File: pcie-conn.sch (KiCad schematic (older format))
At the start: 18 parts, among them J2 1-2199230-6

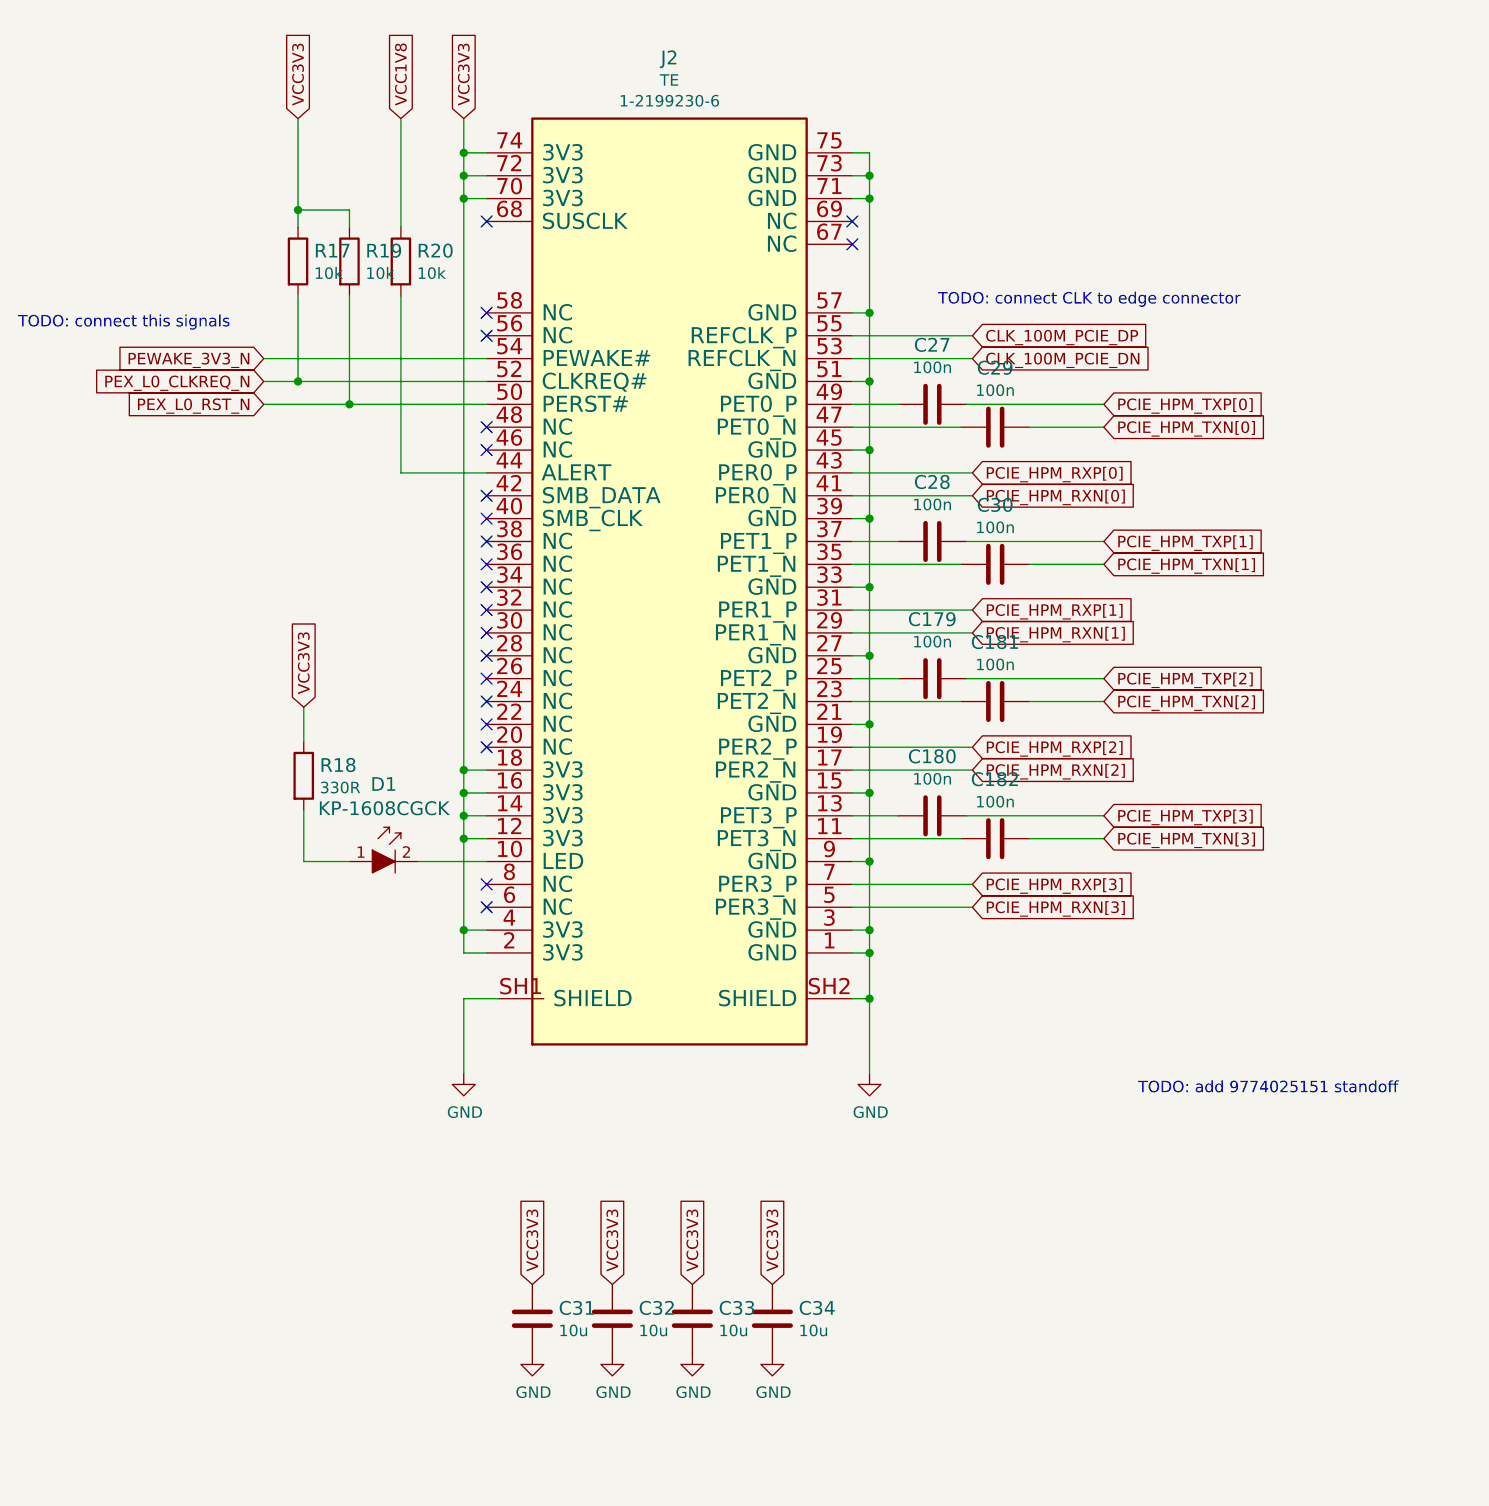
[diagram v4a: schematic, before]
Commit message: Fixes to PCIe connector
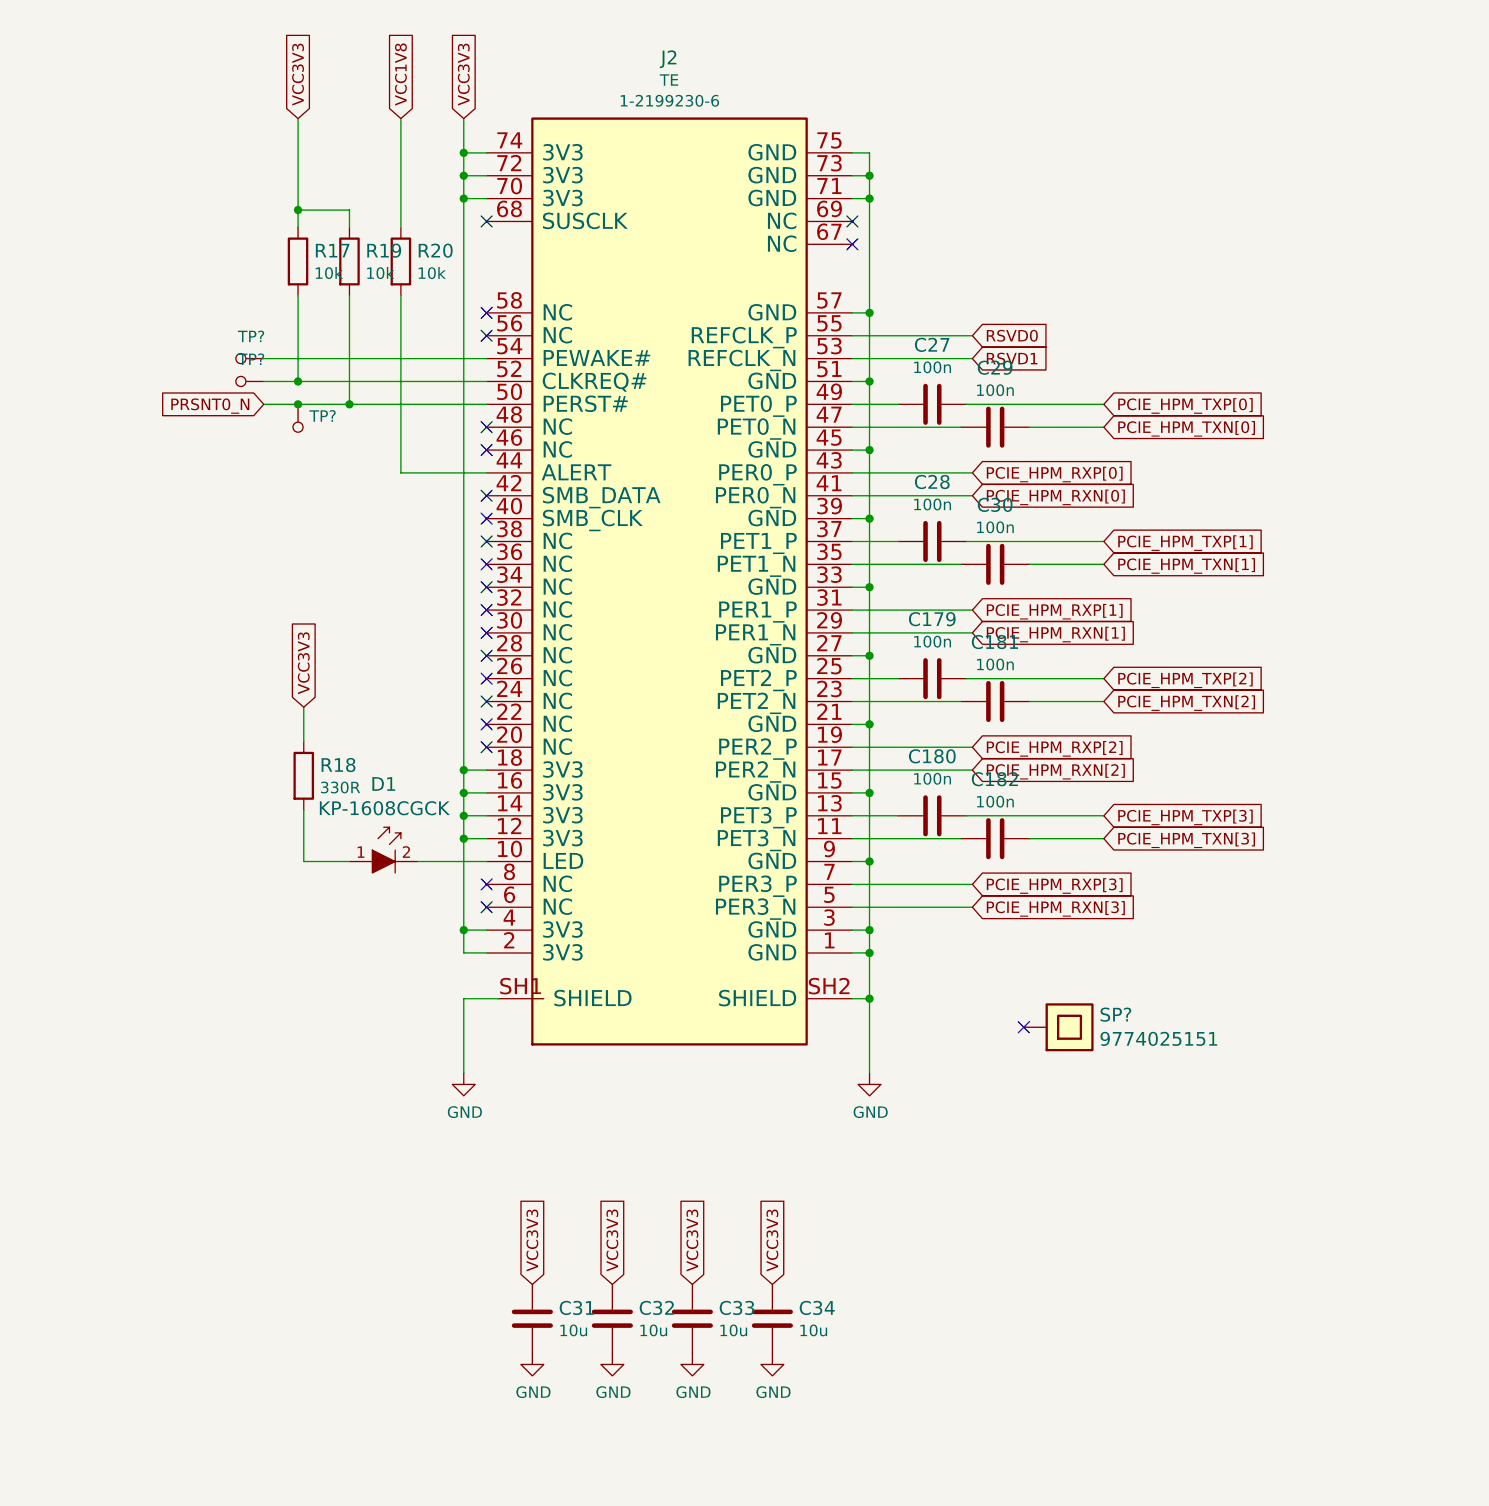
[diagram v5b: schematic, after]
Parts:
- added SP?: 9774025151, antmicro-footprints:9774025151, symbol artix-dc-scm:9774025151
- added TP? (x3): TP_SMD1MM, antmicro-footprints:Testpoint_smd_1mm, symbol artix-dc-scm:TP_SMD1MM
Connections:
- net CLK_100M_PCIE_DN renamed RSVD1
- net CLK_100M_PCIE_DP renamed RSVD0
- net PEWAKE_3V3_N: no longer names the net of J2.54 (PEWAKE#)
- net PEWAKE_3V3_N: now also TP?.1
- net PEX_L0_CLKREQ_N: no longer names the net of J2.52 (CLKREQ#), R17.2
- net PEX_L0_CLKREQ_N: now also TP?.1
- net PEX_L0_RST_N renamed PRSNT0_N
- net PRSNT0_N: now also TP?.1
- no-connect marks 21 -> 22
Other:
- note removed: "TODO: add 9774025151 standoff"
- note removed: "TODO: connect CLK to edge connector\n"
- note removed: "TODO: connect this signals\n"
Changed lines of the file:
@@
 Wire Wire Line
 	7025 3450 7350 3450
-Text GLabel 3675 2550 0    50   Input ~ 0
-PEWAKE_3V3_N
-Text GLabel 3675 2650 0    50   Input ~ 0
-PEX_L0_CLKREQ_N
-Text GLabel 3675 2750 0    50   Input ~ 0
-PEX_L0_RST_N
 Wire Wire Line
 	3675 2550 4650 2550
@@
 	3675 2650 3825 2650
 Wire Wire Line
-	3675 2750 4050 2750
+	3675 2750 3825 2750
 $Comp
 L artix-dc-scm:R_10k_0402 R17
@@
 Text GLabel 5900 6600 1    50   Input ~ 0
 VCC3V3
-Text Notes 7500 5775 0    50   ~ 0
-TODO: add 9774025151 standoff
-Text GLabel 6775 2450 2    50   Input ~ 0
-CLK_100M_PCIE_DP
-Text GLabel 6775 2550 2    50   Input ~ 0
-CLK_100M_PCIE_DN
 NoConn ~ 4650 4950
 NoConn ~ 4650 4850
@@
 Text GLabel 7350 2850 2    50   Input ~ 0
 PCIE_HPM_TXN[0]
-Text Notes 6625 2325 0    50   ~ 0
-TODO: connect CLK to edge connector\n
-Text Notes 2600 2425 0    50   ~ 0
-TODO: connect this signals\n
 Text GLabel 6775 3650 2    50   Input ~ 0
 PCIE_HPM_RXP[1]
@@
 Wire Wire Line
 	7025 4650 7350 4650
+Text GLabel 6775 2450 2    50   Input ~ 0
+RSVD0
+Text GLabel 6775 2550 2    50   Input ~ 0
+RSVD1
+Text GLabel 3675 2750 0    50   Input ~ 0
+PRSNT0_N
+$Comp
+L artix-dc-scm:TP_SMD1MM TP?
+U 1 1 611CC4C6
+P 3575 2550
+F 0 "TP?" V 3480 2597 50  0000 C CNN
+F 1 "TP_SMD1MM" H 3575 2450 50  0001 C CNN
+F 2 "antmicro-footprints:Testpoint_smd_1mm" H 3775 2750 60  0001 L CNN
+F 3 "" H 3775 2850 60  0001 L CNN
+	1    3575 2550
+	0    1    1    0
+$EndComp
+$Comp
+L artix-dc-scm:TP_SMD1MM TP?
+U 1 1 611CCA21
+P 3575 2650
+F 0 "TP?" V 3480 2697 50  0000 C CNN
+F 1 "TP_SMD1MM" H 3575 2550 50  0001 C CNN
+F 2 "antmicro-footprints:Testpoint_smd_1mm" H 3775 2850 60  0001 L CNN
+F 3 "" H 3775 2950 60  0001 L CNN
+	1    3575 2650
+	0    1    1    0
+$EndComp
+$Comp
+L artix-dc-scm:TP_SMD1MM TP?
+U 1 1 611CCE09
+P 3825 2850
+F 0 "TP?" H 3875 2897 50  0000 L CNN
+F 1 "TP_SMD1MM" H 3825 2750 50  0001 C CNN
+F 2 "antmicro-footprints:Testpoint_smd_1mm" H 4025 3050 60  0001 L CNN
+F 3 "" H 4025 3150 60  0001 L CNN
+	1    3825 2850
+	1    0    0    -1
+$EndComp
+Connection ~ 3825 2750
+Wire Wire Line
+	3825 2750 4050 2750
+$Comp
+L artix-dc-scm:9774025151 SP?
+U 1 1 611DD06A
+P 7200 5475
+F 0 "SP?" H 7330 5528 60  0000 L CNN
+F 1 "9774025151" H 7330 5422 60  0000 L CNN
+F 2 "antmicro-footprints:9774025151" H 7200 5475 60  0001 C CNN
+F 3 "" H 7200 5475 60  0001 C CNN
+F 4 "Wurth Elektronik" H 7200 5475 50  0001 C CNN "Manufacturer"
+F 5 "9774025151" H 7200 5475 50  0001 C CNN "MPN"
+	1    7200 5475
+	1    0    0    -1
+$EndComp
+NoConn ~ 7000 5475
 $EndSCHEMATC

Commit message: Fixes after review (pin connections)
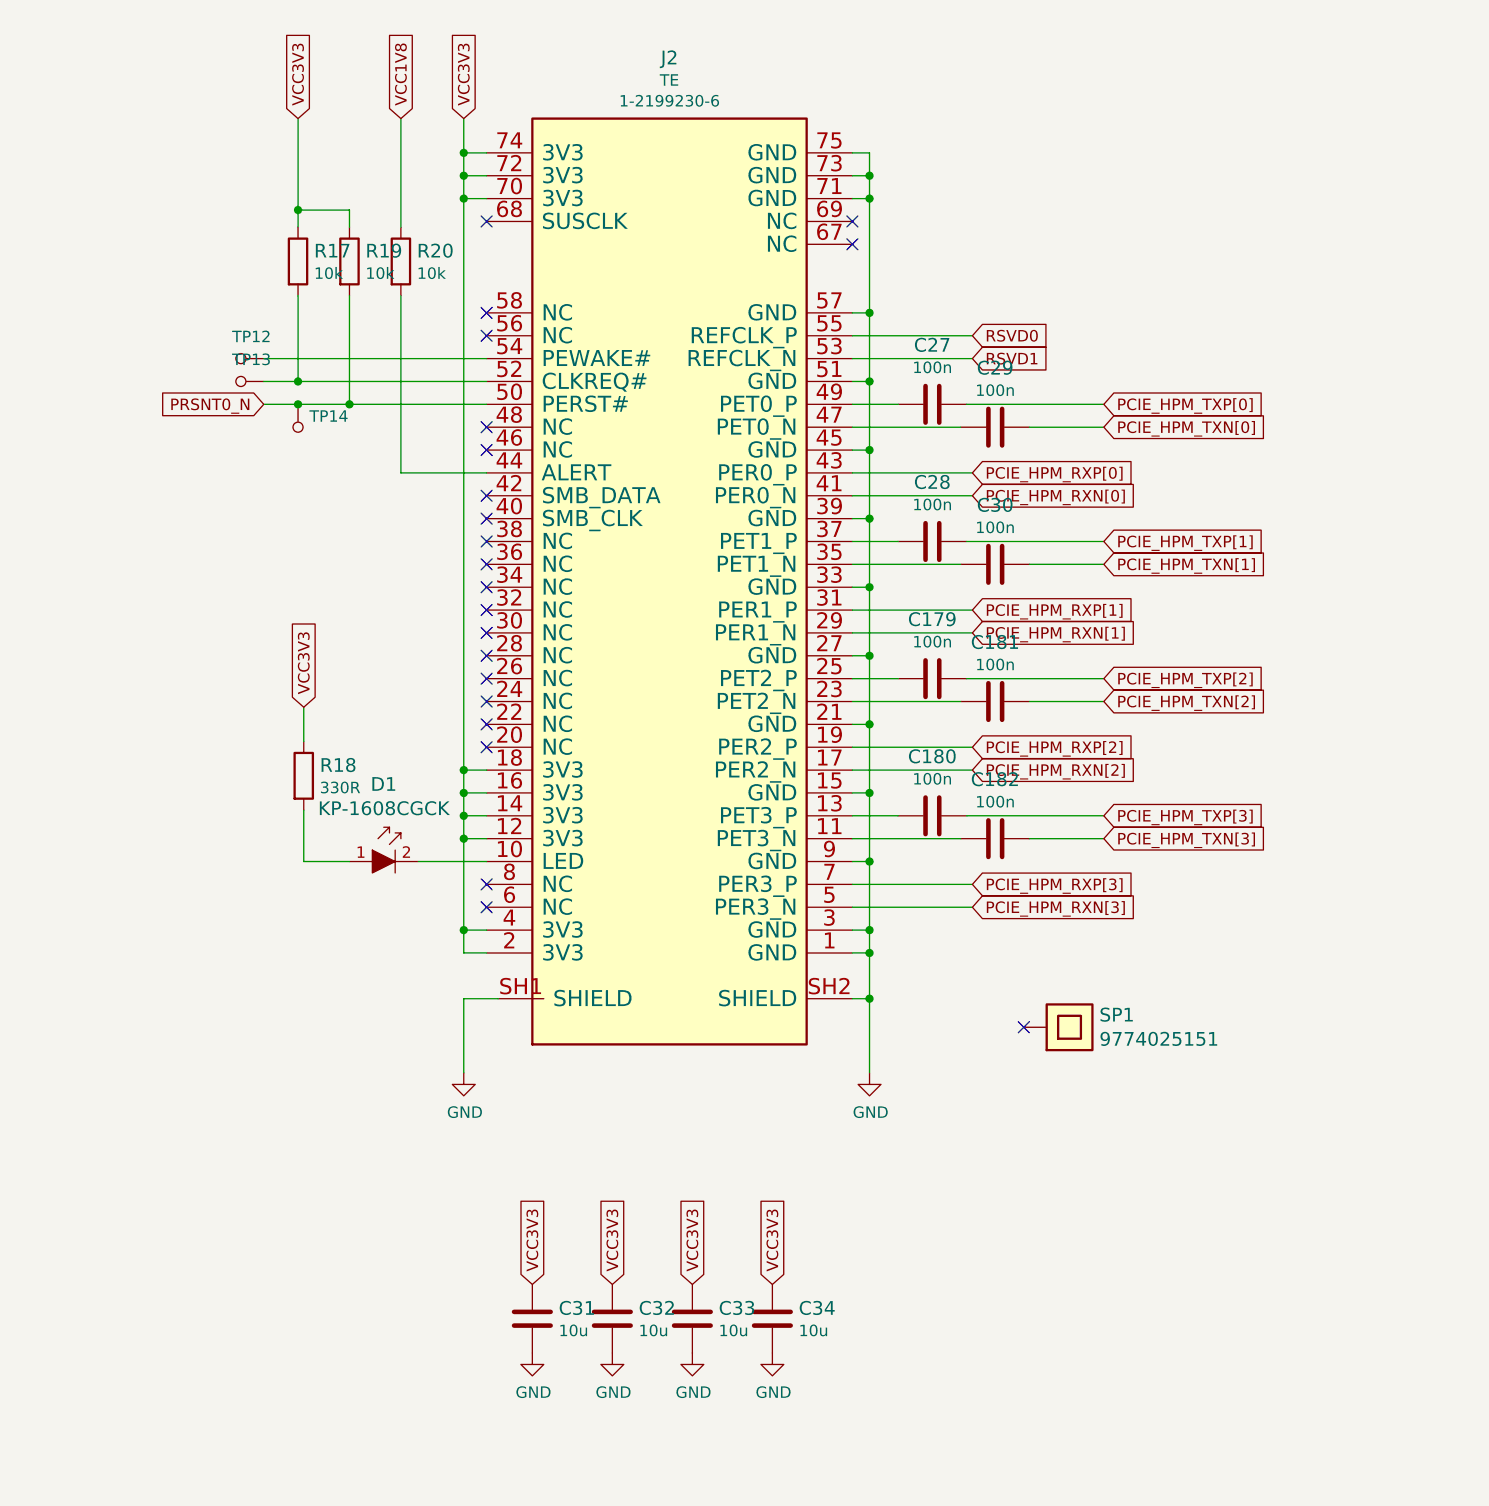
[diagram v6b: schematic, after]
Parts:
- gave numbers to parts that had none: 4
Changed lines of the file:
@@
 PRSNT0_N
 $Comp
-L artix-dc-scm:TP_SMD1MM TP?
+L artix-dc-scm:TP_SMD1MM TP12
 U 1 1 611CC4C6
 P 3575 2550
-F 0 "TP?" V 3480 2597 50  0000 C CNN
+F 0 "TP12" V 3480 2597 50  0000 C CNN
 F 1 "TP_SMD1MM" H 3575 2450 50  0001 C CNN
 F 2 "antmicro-footprints:Testpoint_smd_1mm" H 3775 2750 60  0001 L CNN
@@
 $EndComp
 $Comp
-L artix-dc-scm:TP_SMD1MM TP?
+L artix-dc-scm:TP_SMD1MM TP13
 U 1 1 611CCA21
 P 3575 2650
-F 0 "TP?" V 3480 2697 50  0000 C CNN
+F 0 "TP13" V 3480 2697 50  0000 C CNN
 F 1 "TP_SMD1MM" H 3575 2550 50  0001 C CNN
 F 2 "antmicro-footprints:Testpoint_smd_1mm" H 3775 2850 60  0001 L CNN
@@
 $EndComp
 $Comp
-L artix-dc-scm:TP_SMD1MM TP?
+L artix-dc-scm:TP_SMD1MM TP14
 U 1 1 611CCE09
 P 3825 2850
-F 0 "TP?" H 3875 2897 50  0000 L CNN
+F 0 "TP14" H 3875 2897 50  0000 L CNN
 F 1 "TP_SMD1MM" H 3825 2750 50  0001 C CNN
 F 2 "antmicro-footprints:Testpoint_smd_1mm" H 4025 3050 60  0001 L CNN
@@
 	3825 2750 4050 2750
 $Comp
-L artix-dc-scm:9774025151 SP?
+L artix-dc-scm:9774025151 SP1
 U 1 1 611DD06A
 P 7200 5475
-F 0 "SP?" H 7330 5528 60  0000 L CNN
+F 0 "SP1" H 7330 5528 60  0000 L CNN
 F 1 "9774025151" H 7330 5422 60  0000 L CNN
 F 2 "antmicro-footprints:9774025151" H 7200 5475 60  0001 C CNN

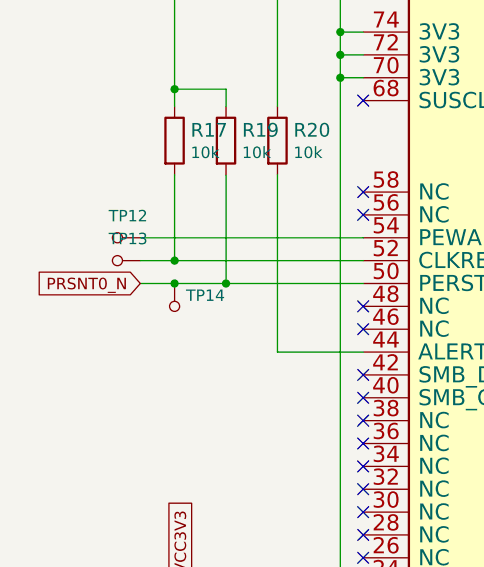
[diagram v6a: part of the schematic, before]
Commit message: Added USB client chip
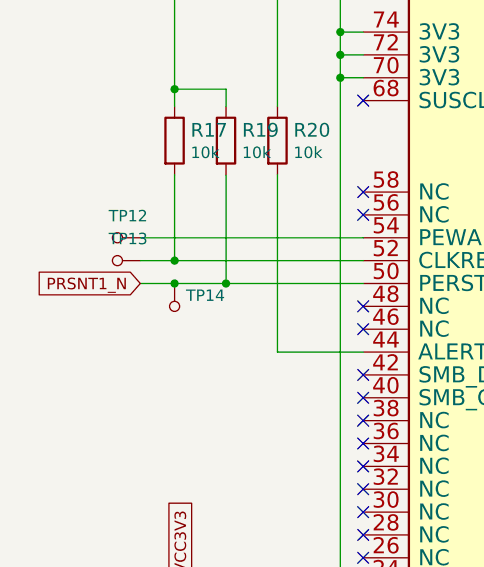
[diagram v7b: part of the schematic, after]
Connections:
- net PRSNT0_N renamed PRSNT1_N
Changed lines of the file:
@@
 RSVD1
 Text GLabel 3675 2750 0    50   Input ~ 0
-PRSNT0_N
+PRSNT1_N
 $Comp
 L artix-dc-scm:TP_SMD1MM TP12

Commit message: Fix in libs
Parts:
- SP1: footprint antmicro-footprints:9774025151 -> artix-dc-scm-footprints:9774025151
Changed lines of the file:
@@
 U 1 1 5FD1CF34
 P 6600 2750
+AR Path="/5FD1CF34" Ref="C27"  Part="1"
+AR Path="/5FD17EF1/5FD1CF34" Ref="C27"  Part="1"
 F 0 "C27" V 6342 2750 60  0000 C CNN
 F 1 "C_100n_0402" H 6600 2600 60  0001 C CNN
@@
 U 1 1 5FD1DAE4
 P 6875 2850
+AR Path="/5FD1DAE4" Ref="C29"  Part="1"
+AR Path="/5FD17EF1/5FD1DAE4" Ref="C29"  Part="1"
 F 0 "C29" V 6617 2850 60  0000 C CNN
 F 1 "C_100n_0402" H 6875 2700 60  0001 C CNN
@@
 U 1 1 5FD279F6
 P 6600 3350
+AR Path="/5FD279F6" Ref="C28"  Part="1"
+AR Path="/5FD17EF1/5FD279F6" Ref="C28"  Part="1"
 F 0 "C28" V 6342 3350 60  0000 C CNN
 F 1 "C_100n_0402" H 6600 3200 60  0001 C CNN
@@
 U 1 1 5FD279FF
 P 6875 3450
+AR Path="/5FD279FF" Ref="C30"  Part="1"
+AR Path="/5FD17EF1/5FD279FF" Ref="C30"  Part="1"
 F 0 "C30" V 6617 3450 60  0000 C CNN
 F 1 "C_100n_0402" H 6875 3300 60  0001 C CNN
@@
 U 1 1 5FFDF949
 P 6600 3950
+AR Path="/5FFDF949" Ref="C179"  Part="1"
+AR Path="/5FD17EF1/5FFDF949" Ref="C179"  Part="1"
 F 0 "C179" V 6342 3950 60  0000 C CNN
 F 1 "C_100n_0402" H 6600 3800 60  0001 C CNN
@@
 U 1 1 5FFDF952
 P 6875 4050
+AR Path="/5FFDF952" Ref="C181"  Part="1"
+AR Path="/5FD17EF1/5FFDF952" Ref="C181"  Part="1"
 F 0 "C181" V 6617 4050 60  0000 C CNN
 F 1 "C_100n_0402" H 6875 3900 60  0001 C CNN
@@
 U 1 1 60013CBE
 P 6600 4550
+AR Path="/60013CBE" Ref="C180"  Part="1"
+AR Path="/5FD17EF1/60013CBE" Ref="C180"  Part="1"
 F 0 "C180" V 6342 4550 60  0000 C CNN
 F 1 "C_100n_0402" H 6600 4400 60  0001 C CNN
@@
 U 1 1 60013CC7
 P 6875 4650
+AR Path="/60013CC7" Ref="C182"  Part="1"
+AR Path="/5FD17EF1/60013CC7" Ref="C182"  Part="1"
 F 0 "C182" V 6617 4650 60  0000 C CNN
 F 1 "C_100n_0402" H 6875 4500 60  0001 C CNN
@@
 F 0 "SP1" H 7330 5528 60  0000 L CNN
 F 1 "9774025151" H 7330 5422 60  0000 L CNN
-F 2 "antmicro-footprints:9774025151" H 7200 5475 60  0001 C CNN
+F 2 "artix-dc-scm-footprints:9774025151" H 7200 5475 60  0001 C CNN
 F 3 "" H 7200 5475 60  0001 C CNN
 F 4 "Wurth Elektronik" H 7200 5475 50  0001 C CNN "Manufacturer"
